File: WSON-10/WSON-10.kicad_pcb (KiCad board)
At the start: 2 copper layers, 13.8 x 16.4 mm, 3 parts, among them J1 Conn_01x06_Male, J2 Conn_01x06_Male, U1 TPS62177DQC

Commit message: get the WSON-10 Working
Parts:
- moved J2 5.11 mm to (77.3, 64.5)
- moved J1 5.05 mm to (57.0, 51.8)
- moved U1 1.27 mm to (67.2, 58.2)
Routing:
- net PAD: track 12.7 -> 4.23 mm
- net VOS: track 4.77 -> 10.4 mm
- net EN: track 4.13 -> 9.71 mm
- net VIN: track 4.97 -> 10.6 mm
- net PGND: track 6.08 -> 11.4 mm
- net SW: track 4.34 -> 9.55 mm
- net nSLEEP: track 5.18 -> 9.76 mm
- net FB: track 5.82 -> 10.3 mm
- net NC: track 4.97 -> 9.50 mm
- net PG: track 7.23 -> 10.6 mm
- net AGND: track 11.2 -> 13.5 mm
- removed copper zone on B.Cu, net PAD
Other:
- board size 13.8 x 16.4 mm -> 24 x 16.4 mm

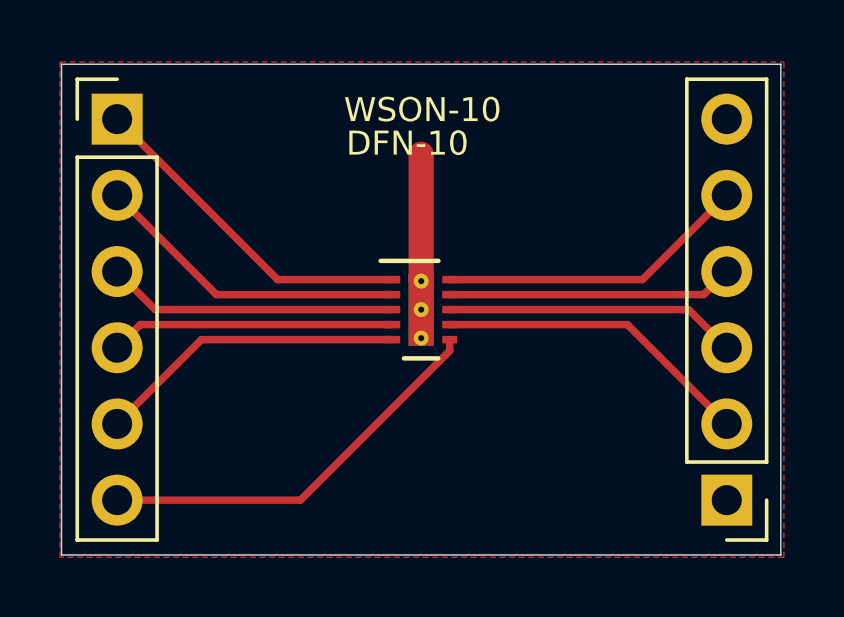
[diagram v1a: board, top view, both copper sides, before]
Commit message: update WSON
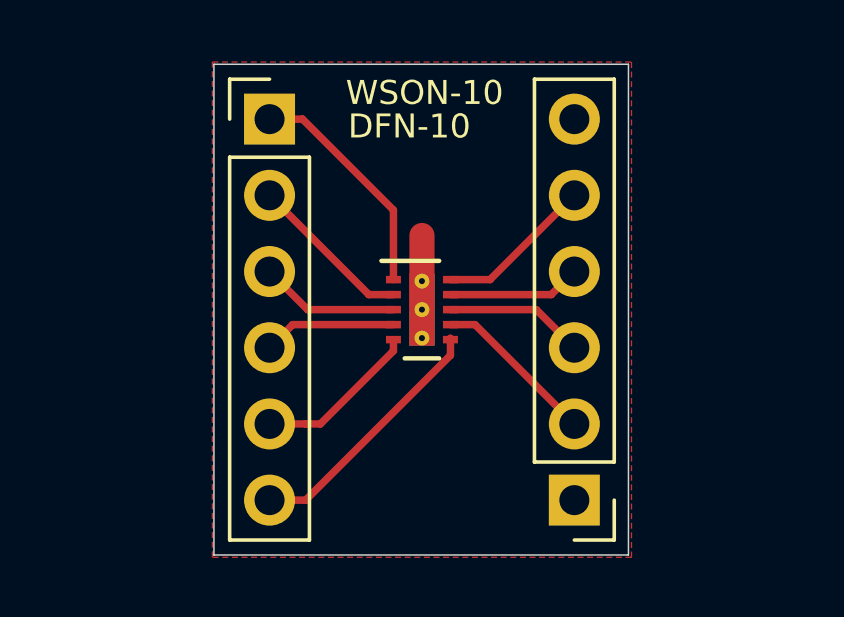
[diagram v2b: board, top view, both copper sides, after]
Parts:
- moved J1 5.08 mm to (62.1, 51.8)
- moved J2 5.08 mm to (72.3, 64.5)
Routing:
- net nSLEEP: track 9.76 -> 4.66 mm
- net SW: track 9.55 -> 4.45 mm
- net VOS: track 10.4 -> 5.29 mm
- net PG: track 10.6 -> 5.50 mm
- net NC: track 9.50 -> 4.45 mm
- net EN: track 9.71 -> 4.66 mm
- net VIN: track 10.6 -> 5.50 mm
- net AGND: track 13.5 -> 8.60 mm
- net FB: track 10.3 -> 5.51 mm
- net PGND: track 11.4 -> 7.71 mm
- net PAD: track 4.23 -> 2.47 mm
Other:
- board size 24 x 16.4 mm -> 13.8 x 16.4 mm
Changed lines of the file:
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@@
     (thickness 1.6)
     (drawings 7)
-    (tracks 22)
+    (tracks 25)
     (zones 0)
     (modules 3)
@@
   )
   (module Package_SON:WSON-10-1EP_2x3mm_P0.5mm_EP0.84x2.4mm_ThermalVias (layer F.Cu)
-    (at 67.1576 58.166)
+    (at 67.183 58.166)
     (descr "WSON-10 package 2x3mm body, pitch 0.5mm, thermal vias and counter-pad, see http://www.ti.com/lit/ds/symlink/tps62177.pdf")
     (tags "WSON 0.5 thermal vias")
@@
   )
   (module Connector_PinHeader_2.54mm:PinHeader_1x06_P2.54mm_Vertical (layer F.Cu)
-    (at 77.343 64.516 180)
+    (at 72.263 64.516 180)
     (descr "Through hole straight pin header, 1x06, 2.54mm pitch, single row")
     (tags "Through hole pin header THT 1x06 2.54mm single row")
@@
   )
   (module Connector_PinHeader_2.54mm:PinHeader_1x06_P2.54mm_Vertical (layer F.Cu)
-    (at 57.023 51.816)
+    (at 62.103 51.816)
     (descr "Through hole straight pin header, 1x06, 2.54mm pitch, single row")
     (tags "Through hole pin header THT 1x06 2.54mm single row")
@@
     (effects (font (size 1.5 1.5) (thickness 0.3)))
   )
-  (gr_line (start 55.1688 66.3448) (end 79.1464 66.3448) (layer Edge.Cuts) (width 0.05))
-  (gr_text DFN-10 (at 66.7004 52.6288) (layer F.SilkS)
+  (gr_line (start 60.2488 66.3448) (end 74.0664 66.3448) (layer Edge.Cuts) (width 0.05))
+  (gr_text DFN-10 (at 66.7639 52.0573) (layer F.SilkS)
     (effects (font (size 0.8 0.8) (thickness 0.15)))
   )
-  (gr_text WSON-10 (at 67.2084 51.5112) (layer F.SilkS)
+  (gr_text WSON-10 (at 67.2719 50.9397) (layer F.SilkS)
     (effects (font (size 0.8 0.8) (thickness 0.15)))
   )
-  (gr_line (start 79.1464 49.9872) (end 55.1688 49.9872) (layer Edge.Cuts) (width 0.05))
-  (gr_line (start 79.1464 66.3448) (end 79.1464 49.9872) (layer Edge.Cuts) (width 0.05))
-  (gr_line (start 55.1688 49.9872) (end 55.1688 66.3448) (layer Edge.Cuts) (width 0.05))
-  (segment (start 67.1576 57.216) (end 67.1576 52.9844) (width 0.84) (layer F.Cu) (net 1))
-  (segment (start 74.533 57.166) (end 77.343 54.356) (width 0.25) (layer F.Cu) (net 2))
-  (segment (start 68.1076 57.166) (end 74.533 57.166) (width 0.25) (layer F.Cu) (net 2))
-  (segment (start 76.573 57.666) (end 77.343 56.896) (width 0.25) (layer F.Cu) (net 3))
-  (segment (start 68.1076 57.666) (end 76.573 57.666) (width 0.25) (layer F.Cu) (net 3))
-  (segment (start 76.073 58.166) (end 77.343 59.436) (width 0.25) (layer F.Cu) (net 4))
-  (segment (start 68.1076 58.166) (end 76.073 58.166) (width 0.25) (layer F.Cu) (net 4))
-  (segment (start 74.033 58.666) (end 77.343 61.976) (width 0.25) (layer F.Cu) (net 5))
-  (segment (start 68.1076 58.666) (end 74.033 58.666) (width 0.25) (layer F.Cu) (net 5))
-  (segment (start 68.1076 59.541) (end 68.1076 59.166) (width 0.25) (layer F.Cu) (net 6))
-  (segment (start 63.1326 64.516) (end 68.1076 59.541) (width 0.25) (layer F.Cu) (net 6))
-  (segment (start 57.023 64.516) (end 63.1326 64.516) (width 0.25) (layer F.Cu) (net 6))
-  (segment (start 59.833 59.166) (end 57.023 61.976) (width 0.25) (layer F.Cu) (net 7))
-  (segment (start 66.2076 59.166) (end 59.833 59.166) (width 0.25) (layer F.Cu) (net 7))
-  (segment (start 58.293 58.166) (end 57.023 56.896) (width 0.25) (layer F.Cu) (net 8))
-  (segment (start 66.2076 58.166) (end 58.293 58.166) (width 0.25) (layer F.Cu) (net 8))
-  (segment (start 60.333 57.666) (end 57.023 54.356) (width 0.25) (layer F.Cu) (net 9))
-  (segment (start 66.2076 57.666) (end 60.333 57.666) (width 0.25) (layer F.Cu) (net 9))
-  (segment (start 62.373 57.166) (end 57.023 51.816) (width 0.25) (layer F.Cu) (net 10))
-  (segment (start 66.2076 57.166) (end 62.373 57.166) (width 0.25) (layer F.Cu) (net 10))
-  (segment (start 57.793 58.666) (end 57.023 59.436) (width 0.25) (layer F.Cu) (net 11))
-  (segment (start 66.2076 58.666) (end 57.793 58.666) (width 0.25) (layer F.Cu) (net 11))
+  (gr_line (start 74.0664 49.9872) (end 60.2488 49.9872) (layer Edge.Cuts) (width 0.05))
+  (gr_line (start 74.0664 66.3448) (end 74.0664 49.9872) (layer Edge.Cuts) (width 0.05))
+  (gr_line (start 60.2488 49.9872) (end 60.2488 66.3448) (layer Edge.Cuts) (width 0.05))
+  (segment (start 67.183 58.166) (end 67.183 55.693919) (width 0.84) (layer F.Cu) (net 1))
+  (segment (start 69.453 57.166) (end 72.263 54.356) (width 0.25) (layer F.Cu) (net 2))
+  (segment (start 68.133 57.166) (end 69.453 57.166) (width 0.25) (layer F.Cu) (net 2))
+  (segment (start 71.493 57.666) (end 72.263 56.896) (width 0.25) (layer F.Cu) (net 3))
+  (segment (start 68.133 57.666) (end 71.493 57.666) (width 0.25) (layer F.Cu) (net 3))
+  (segment (start 70.993 58.166) (end 72.263 59.436) (width 0.25) (layer F.Cu) (net 4))
+  (segment (start 68.133 58.166) (end 70.993 58.166) (width 0.25) (layer F.Cu) (net 4))
+  (segment (start 68.953 58.666) (end 72.263 61.976) (width 0.25) (layer F.Cu) (net 5))
+  (segment (start 68.133 58.666) (end 68.953 58.666) (width 0.25) (layer F.Cu) (net 5))
+  (segment (start 68.133 59.688081) (end 68.133 59.116001) (width 0.25) (layer F.Cu) (net 6))
+  (segment (start 63.305081 64.516) (end 68.133 59.688081) (width 0.25) (layer F.Cu) (net 6))
+  (segment (start 62.103 64.516) (end 63.305081 64.516) (width 0.25) (layer F.Cu) (net 6))
+  (segment (start 63.798 61.976) (end 63.305081 61.976) (width 0.25) (layer F.Cu) (net 7))
+  (segment (start 63.305081 61.976) (end 62.103 61.976) (width 0.25) (layer F.Cu) (net 7))
+  (segment (start 66.233 59.541) (end 63.798 61.976) (width 0.25) (layer F.Cu) (net 7))
+  (segment (start 66.233 59.166) (end 66.233 59.541) (width 0.25) (layer F.Cu) (net 7))
+  (segment (start 63.373 58.166) (end 62.103 56.896) (width 0.25) (layer F.Cu) (net 8))
+  (segment (start 66.233 58.166) (end 63.373 58.166) (width 0.25) (layer F.Cu) (net 8))
+  (segment (start 65.413 57.666) (end 62.103 54.356) (width 0.25) (layer F.Cu) (net 9))
+  (segment (start 66.233 57.666) (end 65.413 57.666) (width 0.25) (layer F.Cu) (net 9))
+  (segment (start 63.203 51.816) (end 62.103 51.816) (width 0.25) (layer F.Cu) (net 10))
+  (segment (start 66.233 54.846) (end 63.203 51.816) (width 0.25) (layer F.Cu) (net 10))
+  (segment (start 66.233 57.166) (end 66.233 54.846) (width 0.25) (layer F.Cu) (net 10))
+  (segment (start 62.873 58.666) (end 62.103 59.436) (width 0.25) (layer F.Cu) (net 11))
+  (segment (start 66.233 58.666) (end 62.873 58.666) (width 0.25) (layer F.Cu) (net 11))
   (zone (net 1) (net_name PAD) (layer F.Cu) (hatch edge 0.508)
     (connect_pads (clearance 0.254))
@@
     (polygon
       (pts
-        (xy 79.248 66.421) (xy 55.118 66.421) (xy 55.118 49.911) (xy 79.248 49.911)
+        (xy 74.168 66.421) (xy 60.198 66.421) (xy 60.198 49.911) (xy 74.168 49.911)
       )
     )
